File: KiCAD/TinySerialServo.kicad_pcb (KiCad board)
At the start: 2 copper layers, 32.8 x 11.7 mm, 24 parts, among them J1 Conn_01x03_Pin, J2 Conn_01x04_Pin, Q1 NPN, SW1 SW_Push, SW2 SW_Push, U1 PIC12LF1840-xSN

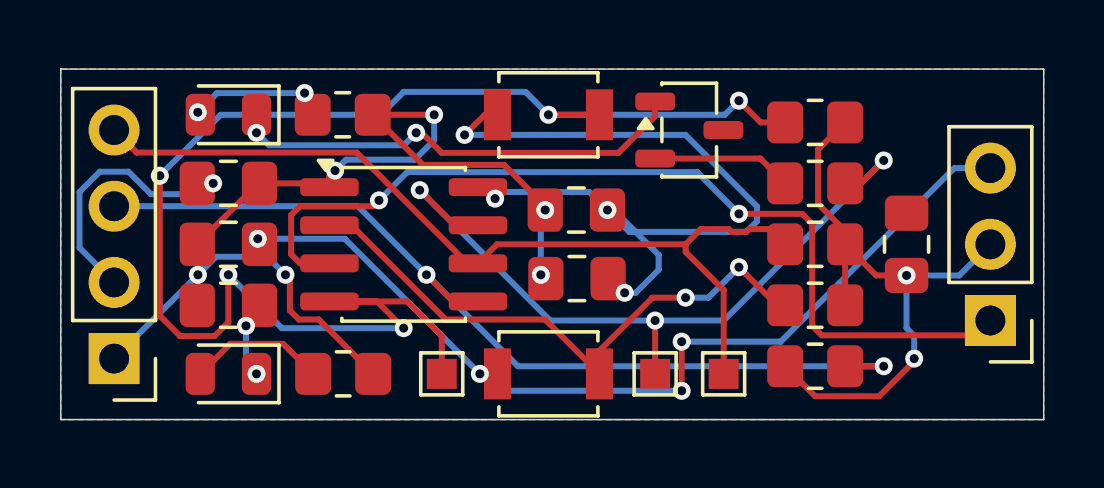
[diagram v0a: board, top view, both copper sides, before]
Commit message: Removed the NPN; Rerouted traces; Remapped pinouts; Changed board dimentions; Added graphics to board
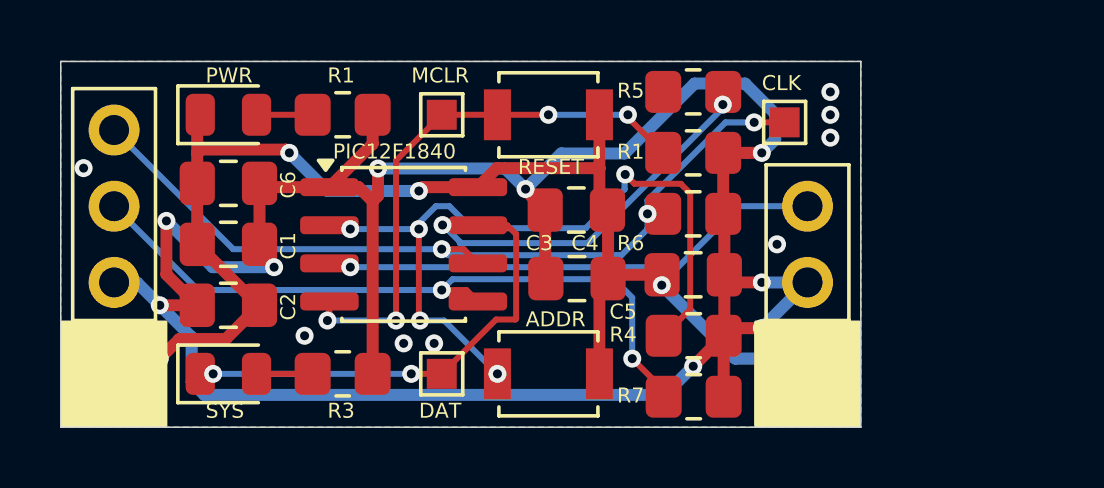
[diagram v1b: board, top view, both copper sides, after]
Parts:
- removed Q1: NPN, Package_TO_SOT_SMD:SOT-23-3
- moved R2 8.64 mm to (163.8, 93.5)
- moved D1 8.64 mm to (160.0, 93.5), turned to 0 degrees
- moved D2 8.64 mm to (160.0, 102.1), turned to 0 degrees
- moved R3 8.64 mm to (163.8, 102.1)
- moved TP1 8.64 mm to (167.1, 93.5)
- moved TP3 8.62 mm to (178.6, 93.7)
- moved C5 7.18 mm to (175.5, 98.8), turned to 180 degrees
- moved TP2 7.11 mm to (167.1, 102.1)
- moved J1 6.23 mm to (179.3, 101.6)
- moved R5 5.08 mm to (175.5, 92.7)
- moved R1 4.19 mm to (175.5, 94.7)
- moved R6 4.19 mm to (175.5, 96.8)
- moved R7 4.17 mm to (175.5, 102.9), turned to 180 degrees
- moved R4 4.17 mm to (175.5, 100.8)
- turned C1 to 180 degrees
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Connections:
- D2 pad 1: Net-(D2-K) -> /SYSLED
- J1 pad 1: /SIG -> /GND
- J1 pad 3: /GND -> /SIG
- J2 pad 1: /VCC -> /GND
- J2 pad 2: /GND -> /VCC
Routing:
- net /MCLR: track 48.4 -> 18.4 mm, vias 5 -> 4
- net /VCC: track 57.2 -> 85.2 mm, vias 8 -> 9
- net /GND: track 70.8 -> 43.8 mm, vias 11 -> 13
- net Net-(D2-K): track 14.9 -> 0.00 mm, vias 2 -> 0
- net /SIG: track 31.1 -> 16.8 mm, vias 2 -> 1
- net /SDA: track 31.2 -> 24.1 mm
- net /BTN: track 19.7 -> 25.6 mm, vias 2 -> 5
- net Net-(Q1-B): track 4.68 -> 0.00 mm
- net /SYSLED: track 25.0 -> 28.3 mm, vias 3 -> 4
- net Net-(D2-A): track 4.66 -> 1.87 mm, vias 2 -> 0
- net Net-(D1-A): track 4.59 -> 1.87 mm
- net /SCL: track 29.6 -> 28.4 mm, vias 0 -> 3
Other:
- board size 32.8 x 11.7 mm -> 26.7 x 12.2 mm
- board text added: "ADDR"
- board text added: "C1"
- board text added: "C2"
- board text added: "C3"
- board text added: "C4"
- board text added: "C5"
- board text added: "C6"
- board text added: "CLK"
- board text added: "DAT"
- board text added: "GND"
- board text added: "I2C Starting ADDR: 0x42 ADDR Btn cycles +15 CMD 0x01 = SetPosition 16bit value"
- board text added: "MCLR"
- board text added: "PIC12F1840"
- board text added: "PWR"
- board text added: "R1"
- board text added: "R3"
- board text added: "R4"
- board text added: "R5"
- board text added: "R6"
- board text added: "R7"
- board text added: "RESET"
- board text added: "SCL"
- board text added: "SDA"
- board text added: "SIG"
- board text added: "SYS"
- board text added: "VCC"

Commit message: PCB Sent to OSH PARK
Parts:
- C1, C3: value C -> 1uF
- C2, C4: value C -> 0.1uF
- C5: value C -> 4.7uF
- C6: value C -> 10uF
- R1, R4: value R -> 10k
- R2: value R -> 1.5k
- R3: value R -> 1k
- R6, R7: value R -> 4.7k
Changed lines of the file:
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@@
 			)
 		)
-		(property "Value" "R"
+		(property "Value" "4.7k"
 			(at 0 1.65 0)
 			(layer "F.Fab")
@@
 			)
 		)
-		(property "Value" "R"
+		(property "Value" "1k"
 			(at 0 1.65 0)
 			(layer "F.Fab")
@@
 			)
 		)
-		(property "Value" "R"
+		(property "Value" "10k"
 			(at 0 1.65 0)
 			(layer "F.Fab")
@@
 			)
 		)
-		(property "Value" "C"
+		(property "Value" "1uF"
 			(at 0 1.68 0)
 			(layer "F.Fab")
@@
 			)
 		)
-		(property "Value" "C"
+		(property "Value" "10uF"
 			(at 0 1.68 0)
 			(layer "F.Fab")
@@
 			)
 		)
-		(property "Value" "C"
+		(property "Value" "4.7uF"
 			(at 0 1.68 0)
 			(layer "F.Fab")
@@
 			)
 		)
-		(property "Value" "C"
+		(property "Value" "0.1uF"
 			(at 0 1.68 0)
 			(layer "F.Fab")
@@
 			)
 		)
-		(property "Value" "R"
+		(property "Value" "1.5k"
 			(at 0 1.65 0)
 			(layer "F.Fab")
@@
 			)
 		)
-		(property "Value" "R"
+		(property "Value" "4.7k"
 			(at 0 1.65 0)
 			(layer "F.Fab")
@@
 			)
 		)
-		(property "Value" "C"
+		(property "Value" "1uF"
 			(at 0 1.68 0)
 			(layer "F.Fab")
@@
 			)
 		)
-		(property "Value" "R"
+		(property "Value" "10k"
 			(at 0 1.65 0)
 			(layer "F.Fab")
@@
 			)
 		)
-		(property "Value" "C"
+		(property "Value" "0.1uF"
 			(at 0 1.68 0)
 			(layer "F.Fab")
